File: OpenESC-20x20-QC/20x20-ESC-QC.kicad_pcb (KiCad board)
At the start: 4 copper layers, 100 x 100 mm, 45 parts

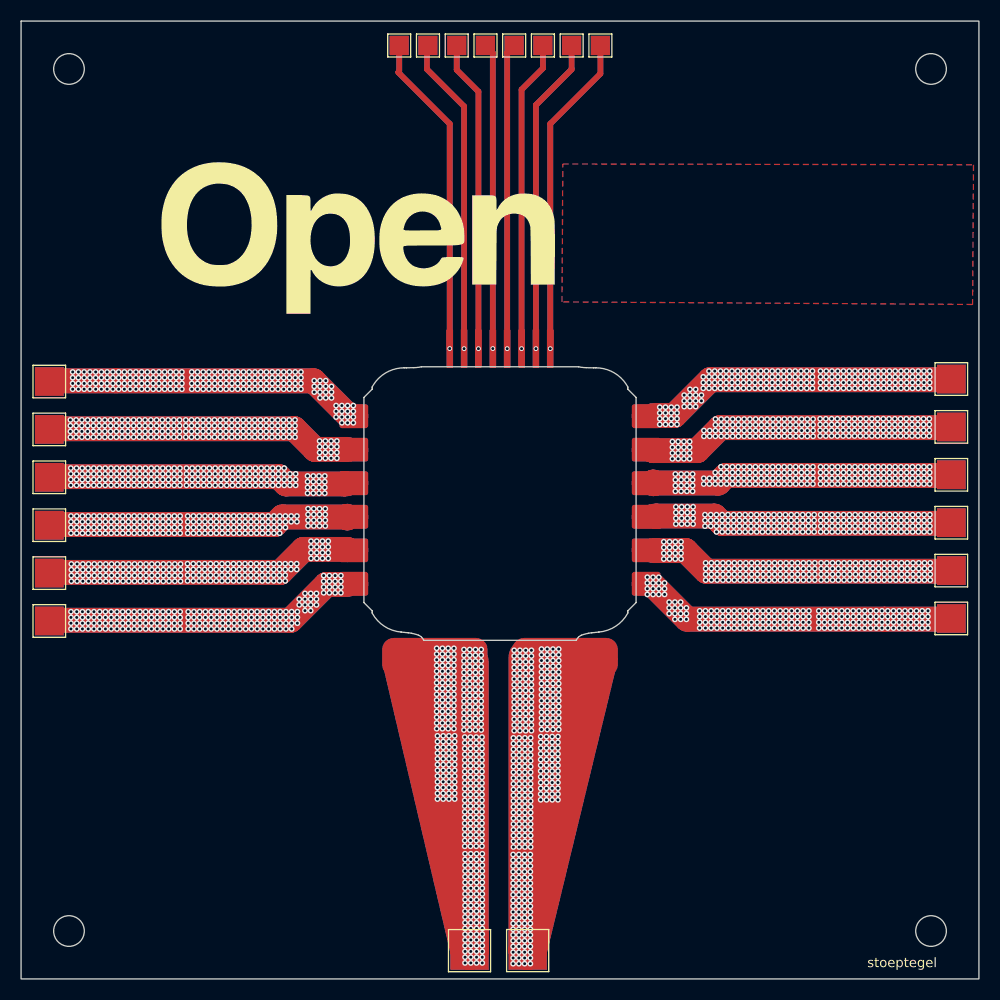
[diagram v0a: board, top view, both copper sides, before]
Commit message: Rev 3.1 working state: flashing fixture, QC updates, board work
New 20x20-ESC-Flashing pogo-pin fixture project, MotorTest project file,
QC fixture and main board PCB updates, shop badge on the new gold.
Internal notes and regenerable fixture STEPs stay local via the
repo-specific .gitignore tail.

Co-Authored-By: Claude Opus 5 (1M context) <noreply@anthropic.com>
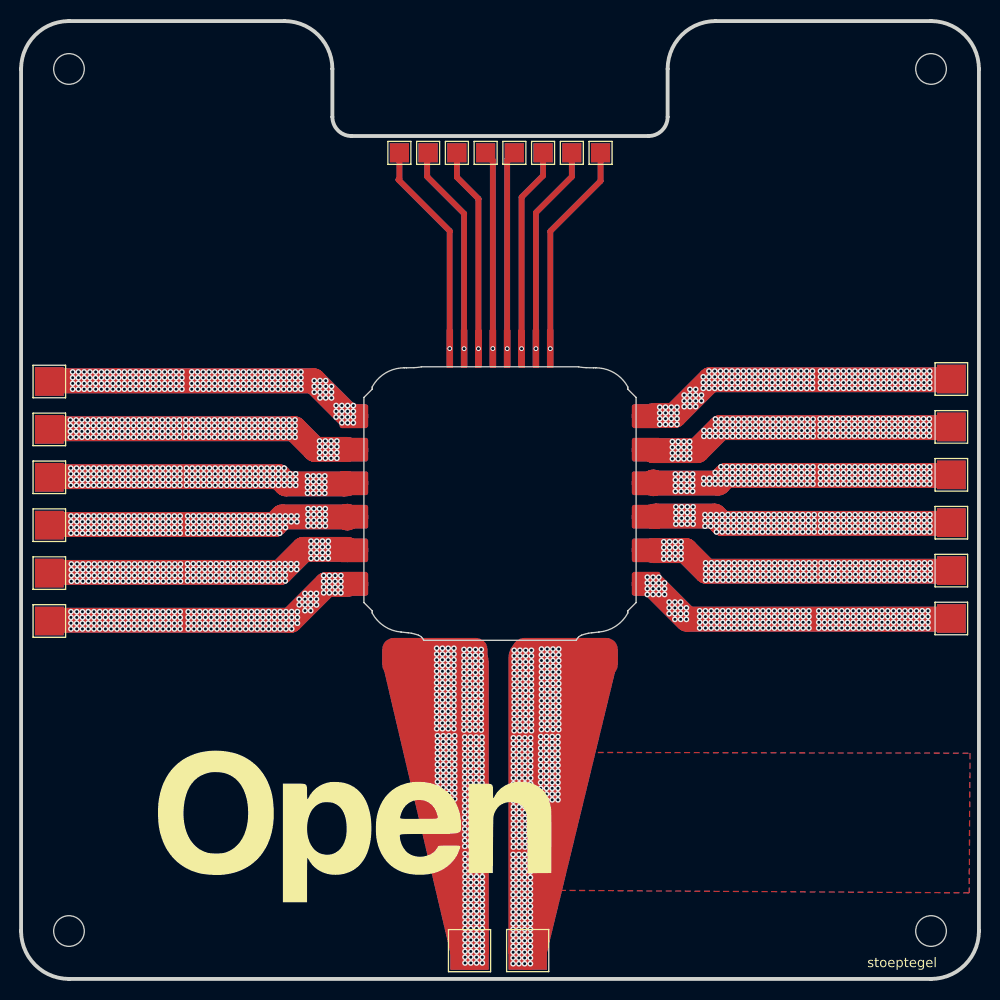
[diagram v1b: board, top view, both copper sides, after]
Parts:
- moved REF** 11.2 mm to (125.8, 56.8)
- moved REF**10 11.2 mm to (110.8, 56.8)
- moved REF**11 11.2 mm to (107.8, 56.8)
- moved REF**12 11.2 mm to (104.8, 56.8)
- moved REF**6 11.2 mm to (122.8, 56.8)
- moved REF**7 11.2 mm to (119.8, 56.8)
- moved REF**8 11.2 mm to (116.8, 56.8)
- moved REF**9 11.2 mm to (113.8, 56.8)
- moved REF** 11.2 mm to (104.8, 56.8)
- moved REF**10 11.2 mm to (119.8, 56.8)
- moved REF**11 11.2 mm to (122.8, 56.8)
- moved REF**12 11.2 mm to (125.8, 56.8)
- moved REF**6 11.2 mm to (107.8, 56.8)
- moved REF**7 11.2 mm to (110.8, 56.8)
- moved REF**8 11.2 mm to (113.8, 56.8)
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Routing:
- net (no net): track 2074.9 -> 1895.5 mm
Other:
- outline, holes or cut-outs redrawn
